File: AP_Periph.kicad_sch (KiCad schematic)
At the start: 15 parts, among them J5 Conn_ARM_SWD_TagConnect_TC203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, U4 STM32L431CCUx, X1 ECS-2520MVLC-080-BP-TR

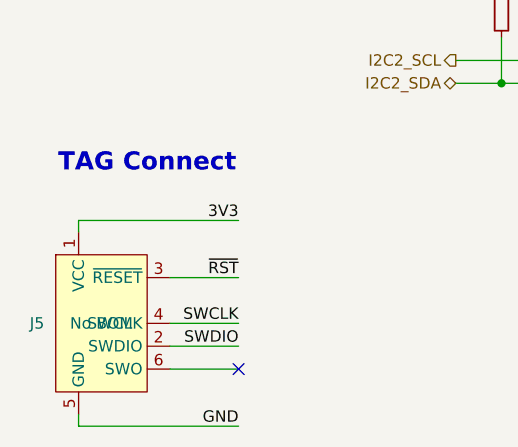
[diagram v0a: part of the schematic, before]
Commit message: Update to 6 pin headers and remove the two solder pads
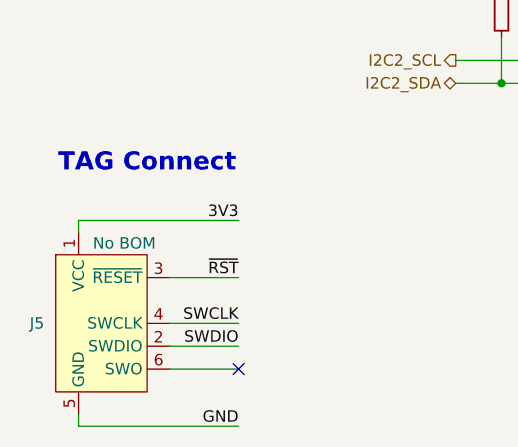
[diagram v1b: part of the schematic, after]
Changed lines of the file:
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@@
 		(on_board yes)
 		(dnp no)
-		(fields_autoplaced yes)
 		(property "Reference" "J5"
 			(at 38.1 146.0499 0)
@@
 		)
 		(property "Notes" "No BOM"
-			(at 44.45 146.05 0)
+			(at 46.99 137.16 0)
 			(effects
 				(font
